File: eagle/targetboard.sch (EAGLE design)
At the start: 80 parts, among them CN1 DIP-BLACK-MALE-HEADER-VERT(3P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, IC1 MCP2551, IC2 LPC1768 or LPC1768, IC3 PMIC-CJT1117-3.3(SOT223), IC4 MCP2551, IC5 TB6612FNG, IC6 TB6612FNG, IC7 MAX232D, J1 DIP-BLACK-MALE-HEADER-VERT(8P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, J10 CAN1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

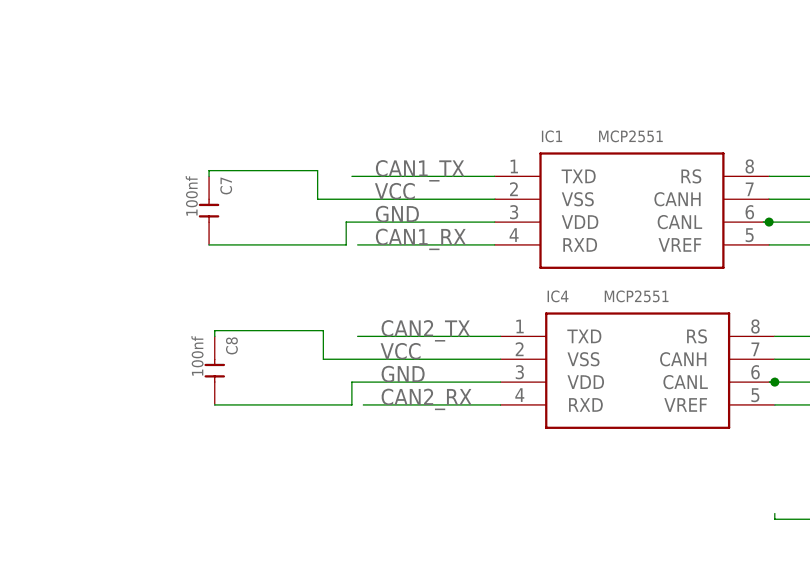
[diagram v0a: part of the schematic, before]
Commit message: Fix Board revision, CAN VCC and VSS mixed up
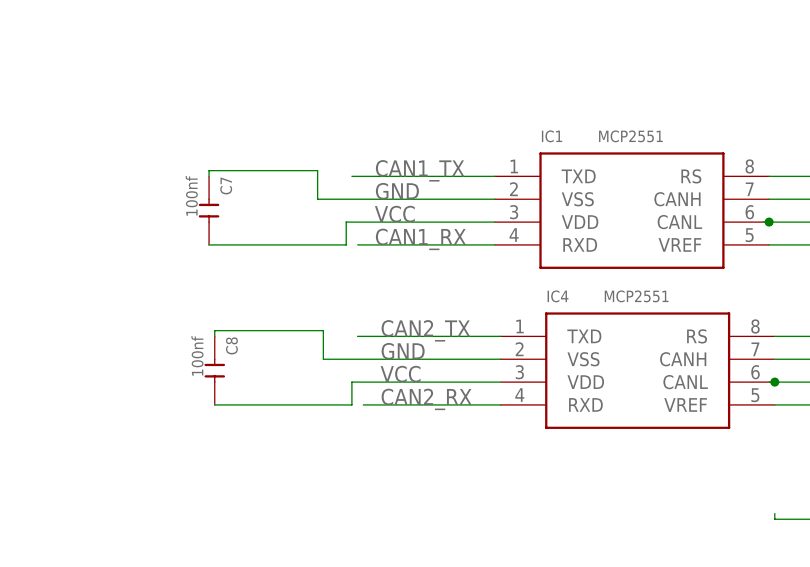
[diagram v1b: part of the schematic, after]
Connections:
- net GND: now also C7.1, C8.1, IC1.VSS, IC4.VSS; no longer C7.2, C8.2, IC1.VDD, IC4.VDD
- net VCC: now also C7.2, C8.2, IC1.VDD, IC4.VDD; no longer C7.1, C8.1, IC1.VSS, IC4.VSS
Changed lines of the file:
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@@
-</segment>
-<segment>
-<pinref part="IC1" gate="G$1" pin="VDD"/>
-<wire x1="76.2" y1="186.055" x2="59.69" y2="186.055" width="0.1524" layer="91"/>
-<label x="62.865" y="186.055" size="1.778" layer="95"/>
-<wire x1="44.45" y1="183.515" x2="59.69" y2="183.515" width="0.1524" layer="91"/>
-<wire x1="59.69" y1="183.515" x2="59.69" y2="186.055" width="0.1524" layer="91"/>
-<pinref part="C7" gate="G$1" pin="2"/>
-</segment>
-<segment>
-<pinref part="IC4" gate="G$1" pin="VDD"/>
-<wire x1="76.835" y1="168.275" x2="60.325" y2="168.275" width="0.1524" layer="91"/>
-<label x="63.5" y="168.275" size="1.778" layer="95"/>
-<wire x1="45.085" y1="165.735" x2="60.325" y2="165.735" width="0.1524" layer="91"/>
-<wire x1="60.325" y1="165.735" x2="60.325" y2="168.275" width="0.1524" layer="91"/>
-<pinref part="C8" gate="G$1" pin="2"/>
 </segment>
 <segment>
@@
 <wire x1="268.605" y1="18.415" x2="268.605" y2="19.05" width="0.1524" layer="91"/>
 <label x="263.525" y="19.05" size="1.778" layer="95"/>
+</segment>
+<segment>
+<pinref part="IC1" gate="G$1" pin="VSS"/>
+<wire x1="76.2" y1="188.595" x2="56.515" y2="188.595" width="0.1524" layer="91"/>
+<label x="62.865" y="188.595" size="1.778" layer="95"/>
+<wire x1="56.515" y1="188.595" x2="56.515" y2="191.77" width="0.1524" layer="91"/>
+<pinref part="C7" gate="G$1" pin="1"/>
+<wire x1="56.515" y1="191.77" x2="44.45" y2="191.77" width="0.1524" layer="91"/>
+<wire x1="44.45" y1="191.77" x2="44.45" y2="191.135" width="0.1524" layer="91"/>
+</segment>
+<segment>
+<pinref part="IC4" gate="G$1" pin="VSS"/>
+<wire x1="76.835" y1="170.815" x2="57.15" y2="170.815" width="0.1524" layer="91"/>
+<label x="63.5" y="170.815" size="1.778" layer="95"/>
+<wire x1="57.15" y1="170.815" x2="57.15" y2="173.99" width="0.1524" layer="91"/>
+<pinref part="C8" gate="G$1" pin="1"/>
+<wire x1="57.15" y1="173.99" x2="45.085" y2="173.99" width="0.1524" layer="91"/>
+<wire x1="45.085" y1="173.99" x2="45.085" y2="173.355" width="0.1524" layer="91"/>
 </segment>
 </net>
@@
 </segment>
 <segment>
-<pinref part="IC1" gate="G$1" pin="VSS"/>
-<wire x1="76.2" y1="188.595" x2="56.515" y2="188.595" width="0.1524" layer="91"/>
-<label x="62.865" y="188.595" size="1.778" layer="95"/>
-<wire x1="56.515" y1="188.595" x2="56.515" y2="191.77" width="0.1524" layer="91"/>
-<pinref part="C7" gate="G$1" pin="1"/>
-<wire x1="56.515" y1="191.77" x2="44.45" y2="191.77" width="0.1524" layer="91"/>
-<wire x1="44.45" y1="191.77" x2="44.45" y2="191.135" width="0.1524" layer="91"/>
-</segment>
-<segment>
-<pinref part="IC4" gate="G$1" pin="VSS"/>
-<wire x1="76.835" y1="170.815" x2="57.15" y2="170.815" width="0.1524" layer="91"/>
-<label x="63.5" y="170.815" size="1.778" layer="95"/>
-<wire x1="57.15" y1="170.815" x2="57.15" y2="173.99" width="0.1524" layer="91"/>
-<pinref part="C8" gate="G$1" pin="1"/>
-<wire x1="57.15" y1="173.99" x2="45.085" y2="173.99" width="0.1524" layer="91"/>
-<wire x1="45.085" y1="173.99" x2="45.085" y2="173.355" width="0.1524" layer="91"/>
-</segment>
-<segment>
 <pinref part="R11" gate="G$1" pin="2"/>
 <pinref part="P+5" gate="VCC" pin="VCC"/>
@@
 <label x="-67.31" y="252.73" size="1.778" layer="95"/>
 </segment>
+<segment>
+<pinref part="IC1" gate="G$1" pin="VDD"/>
+<wire x1="76.2" y1="186.055" x2="59.69" y2="186.055" width="0.1524" layer="91"/>
+<label x="62.865" y="186.055" size="1.778" layer="95"/>
+<wire x1="44.45" y1="183.515" x2="59.69" y2="183.515" width="0.1524" layer="91"/>
+<wire x1="59.69" y1="183.515" x2="59.69" y2="186.055" width="0.1524" layer="91"/>
+<pinref part="C7" gate="G$1" pin="2"/>
+</segment>
+<segment>
+<pinref part="IC4" gate="G$1" pin="VDD"/>
+<wire x1="76.835" y1="168.275" x2="60.325" y2="168.275" width="0.1524" layer="91"/>
+<label x="63.5" y="168.275" size="1.778" layer="95"/>
+<wire x1="45.085" y1="165.735" x2="60.325" y2="165.735" width="0.1524" layer="91"/>
+<wire x1="60.325" y1="165.735" x2="60.325" y2="168.275" width="0.1524" layer="91"/>
+<pinref part="C8" gate="G$1" pin="2"/>
+</segment>
 </net>
